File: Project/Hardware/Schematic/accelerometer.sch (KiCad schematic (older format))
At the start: 2 parts

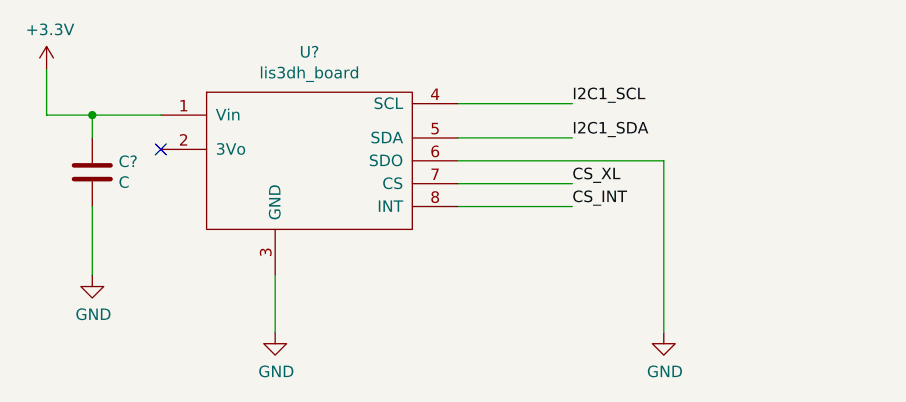
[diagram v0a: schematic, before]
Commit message: Ändrade CS-pin på accelerometern, lade till kommentarer och värde på bypassen.
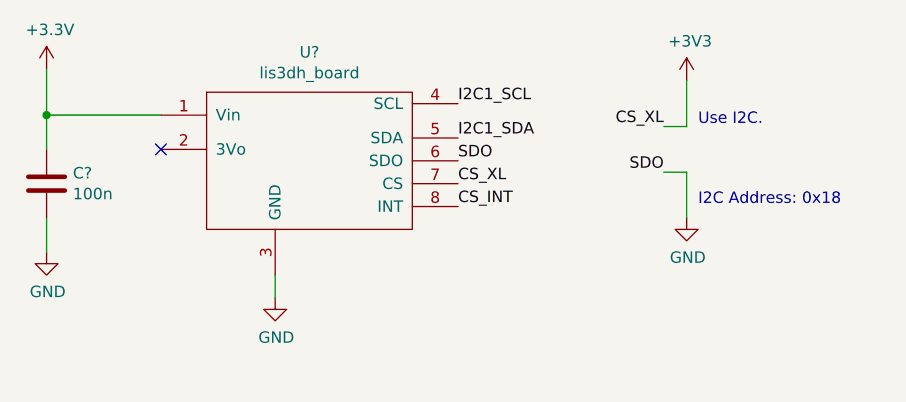
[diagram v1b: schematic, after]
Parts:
- C?: value C -> 100n
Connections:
- net CS_XL is gone; now on net +3V3: U?.7 (CS)
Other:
- note added: "I2C Address: 0x18"
- note added: "Use I2C."
- moved on the sheet: C?
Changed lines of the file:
@@
 $EndComp
 Wire Wire Line
-	6700 3150 6400 3150
+	6700 3150 6200 3150
 $Comp
 L power:GND #PWR?
 U 1 1 5C59F3FC
-P 7200 4100
-F 0 "#PWR?" H 7200 3850 50  0001 C CNN
-F 1 "GND" H 7205 3927 50  0000 C CNN
-F 2 "" H 7200 4100 50  0001 C CNN
-F 3 "" H 7200 4100 50  0001 C CNN
-	1    7200 4100
+P 7200 3950
+F 0 "#PWR?" H 7200 3700 50  0001 C CNN
+F 1 "GND" H 7205 3777 50  0000 C CNN
+F 2 "" H 7200 3950 50  0001 C CNN
+F 3 "" H 7200 3950 50  0001 C CNN
+	1    7200 3950
 	1    0    0    -1
 $EndComp
 Wire Wire Line
-	7200 3850 7200 4100
+	7200 3850 7200 3950
 $Comp
 L power:GND #PWR?
 U 1 1 5C59F76F
-P 8900 4100
-F 0 "#PWR?" H 8900 3850 50  0001 C CNN
-F 1 "GND" H 8905 3927 50  0000 C CNN
-F 2 "" H 8900 4100 50  0001 C CNN
-F 3 "" H 8900 4100 50  0001 C CNN
-	1    8900 4100
+P 9000 3600
+F 0 "#PWR?" H 9000 3350 50  0001 C CNN
+F 1 "GND" H 9005 3427 50  0000 C CNN
+F 2 "" H 9000 3600 50  0001 C CNN
+F 3 "" H 9000 3600 50  0001 C CNN
+	1    9000 3600
 	1    0    0    -1
 $EndComp
-Wire Wire Line
-	8900 3350 8900 4100
 NoConn ~ 6700 3300
-Wire Wire Line
-	8000 3100 8500 3100
-Text Label 8500 3100 0    50   ~ 0
+Text Label 8000 3100 0    50   ~ 0
 I2C1_SCL
-Wire Wire Line
-	8000 3250 8500 3250
-Text Label 8500 3250 0    50   ~ 0
+Text Label 8000 3250 0    50   ~ 0
 I2C1_SDA
-Wire Wire Line
-	8000 3350 8900 3350
-Wire Wire Line
-	8000 3550 8500 3550
-Text Label 8500 3550 0    50   ~ 0
+Text Label 8000 3550 0    50   ~ 0
 CS_INT
-Wire Wire Line
-	8000 3450 8500 3450
-Text Label 8500 3450 0    50   ~ 0
-CS_XL
 $Comp
 L Device:C C?
 U 1 1 5C5A61DB
-P 6400 3400
-F 0 "C?" H 6515 3446 50  0000 L CNN
-F 1 "C" H 6515 3355 50  0000 L CNN
-F 2 "" H 6438 3250 50  0001 C CNN
-F 3 "~" H 6400 3400 50  0001 C CNN
-	1    6400 3400
+P 6200 3450
+F 0 "C?" H 6315 3496 50  0000 L CNN
+F 1 "100n" H 6315 3405 50  0000 L CNN
+F 2 "" H 6238 3300 50  0001 C CNN
+F 3 "~" H 6200 3450 50  0001 C CNN
+	1    6200 3450
 	1    0    0    -1
 $EndComp
@@
 L power:GND #PWR?
 U 1 1 5C5A62A1
-P 6400 3850
-F 0 "#PWR?" H 6400 3600 50  0001 C CNN
-F 1 "GND" H 6405 3677 50  0000 C CNN
-F 2 "" H 6400 3850 50  0001 C CNN
-F 3 "" H 6400 3850 50  0001 C CNN
-	1    6400 3850
+P 6200 3750
+F 0 "#PWR?" H 6200 3500 50  0001 C CNN
+F 1 "GND" H 6205 3577 50  0000 C CNN
+F 2 "" H 6200 3750 50  0001 C CNN
+F 3 "" H 6200 3750 50  0001 C CNN
+	1    6200 3750
 	1    0    0    -1
 $EndComp
 Wire Wire Line
-	6400 3150 6400 3250
-Connection ~ 6400 3150
+	6200 3150 6200 3300
+Connection ~ 6200 3150
 Wire Wire Line
-	6400 3150 6200 3150
+	6200 3600 6200 3750
+Text Notes 9050 3550 0    50   ~ 0
+I2C Address: 0x18
+Text Label 8000 3350 0    50   ~ 0
+SDO
 Wire Wire Line
-	6400 3550 6400 3850
+	9000 3400 8900 3400
+Wire Wire Line
+	9000 3400 9000 3600
+Text Label 8900 3400 2    50   ~ 0
+SDO
+Text Label 8000 3450 0    50   ~ 0
+CS_XL
+$Comp
+L power:+3V3 #PWR?
+U 1 1 5C5D1727
+P 9000 3000
+F 0 "#PWR?" H 9000 2850 50  0001 C CNN
+F 1 "+3V3" H 9015 3173 50  0000 C CNN
+F 2 "" H 9000 3000 50  0001 C CNN
+F 3 "" H 9000 3000 50  0001 C CNN
+	1    9000 3000
+	1    0    0    -1
+$EndComp
+Wire Wire Line
+	9000 3000 9000 3200
+Wire Wire Line
+	9000 3200 8900 3200
+Text Label 8900 3200 2    50   ~ 0
+CS_XL
+Text Notes 9050 3200 0    50   ~ 0
+Use I2C.
 $EndSCHEMATC

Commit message: Pulse, piezo och labels (#8)
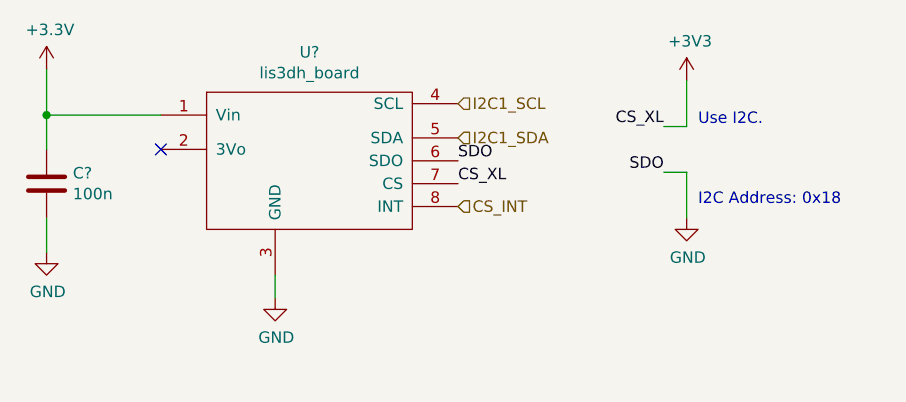
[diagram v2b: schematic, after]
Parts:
- removed U?: lis3dh_board, symbol PASC:lis3dh_board
- added U?: lis3dh_board, symbol PASC:lis3dh_board
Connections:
- net +3V3: now also U?.1 (Vin), U?.7 (CS)
- net CS_INT: now also U?.8 (INT)
- net GND: now also U?.3 (GND), U?.6 (SDO)
- net I2C1_SCL: now also U?.4 (SCL)
- net I2C1_SDA: now also U?.5 (SDA)
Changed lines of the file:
@@
 Wire Wire Line
 	6200 2950 6200 3150
-$Comp
-L PASC:lis3dh_board U?
-U 1 1 5C59F00B
-P 7350 3350
-F 0 "U?" H 7350 3825 50  0000 C CNN
-F 1 "lis3dh_board" H 7350 3734 50  0000 C CNN
-F 2 "" H 7350 3350 50  0001 C CNN
-F 3 "" H 7350 3350 50  0001 C CNN
-	1    7350 3350
-	1    0    0    -1
-$EndComp
 Wire Wire Line
 	6700 3150 6200 3150
@@
 $EndComp
 NoConn ~ 6700 3300
-Text Label 8000 3100 0    50   ~ 0
-I2C1_SCL
-Text Label 8000 3250 0    50   ~ 0
-I2C1_SDA
-Text Label 8000 3550 0    50   ~ 0
-CS_INT
 $Comp
 L Device:C C?
@@
 Text Notes 9050 3200 0    50   ~ 0
 Use I2C.
+Text HLabel 8000 3100 2    50   Input ~ 0
+I2C1_SCL
+Text HLabel 8000 3250 2    50   Input ~ 0
+I2C1_SDA
+Text HLabel 8000 3550 2    50   Input ~ 0
+CS_INT
+$Comp
+L PASC:lis3dh_board U?
+U 1 1 5C5E039C
+P 7350 3350
+F 0 "U?" H 7350 3825 50  0000 C CNN
+F 1 "lis3dh_board" H 7350 3734 50  0000 C CNN
+F 2 "" H 7350 3350 50  0001 C CNN
+F 3 "" H 7350 3350 50  0001 C CNN
+	1    7350 3350
+	1    0    0    -1
+$EndComp
 $EndSCHEMATC

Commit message: La till pins till cubemx, bytte transistor till piezo och la till footprint för accelerometer
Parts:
- U?: footprint (none) -> PASC:LIS3DH
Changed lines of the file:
@@
 F 0 "U?" H 7350 3825 50  0000 C CNN
 F 1 "lis3dh_board" H 7350 3734 50  0000 C CNN
-F 2 "" H 7350 3350 50  0001 C CNN
+F 2 "PASC:LIS3DH" H 7350 3350 50  0001 C CNN
 F 3 "" H 7350 3350 50  0001 C CNN
 	1    7350 3350
